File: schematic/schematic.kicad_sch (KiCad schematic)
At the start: 0 parts

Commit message: a
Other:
- title: (none) -> Overview
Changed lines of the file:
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@@
 (kicad_sch (version 20211123) (generator eeschema)
   (paper "USLetter")
+  (title_block
+    (title "Overview")
+    (date "2022-03-18")
+    (comment 1 "Engineer/Draftsman: Joesphan Lu")
+  )
   (junction (at 82.55 49.53) (diameter 0) (color 0 0 0 0)
   )
@@
       (reference "#PWR0178") (unit 1) (value "GND") (footprint "")
     )
+    (path "/00000000-0000-0000-0000-00006200d680/56a155f6-67fb-4ed4-abee-b01de92744a0"
+      (reference "#PWR?") (unit 1) (value "Vdrive") (footprint "")
+    )
     (path "/00000000-0000-0000-0000-000061f58c1a/00000000-0000-0000-0000-000062198c67"

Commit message: e
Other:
- sheet MCU ports: added DRIVER; removed DRIVER_P, MOS_VDRIVE_PWM
- sheet Peltier Driver ports: added DRIVER; removed CHG_PUMP_PWM, DRIVER_N, DRIVER_P
- sheet Power Management ports: added 5V; removed none

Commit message: d
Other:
- sheet ports renamed Human Interface
- sheet Human Interface: file ports.kicad_sch -> HI.kicad_sch
- sheet Human Interface ports: added none; removed PELTIER_N, PELTIER_P
- sheet MCU ports: added ~DRIVER_DIR, ~DRIVER_EN; removed DRIVER, DRIVER_N
- sheet Peltier Driver ports: added 5V, ~DRIVER_DIR, ~DRIVER_EN; removed DRIVER, MOS_VDRIVE, PELTIER_N, PELTIER_P

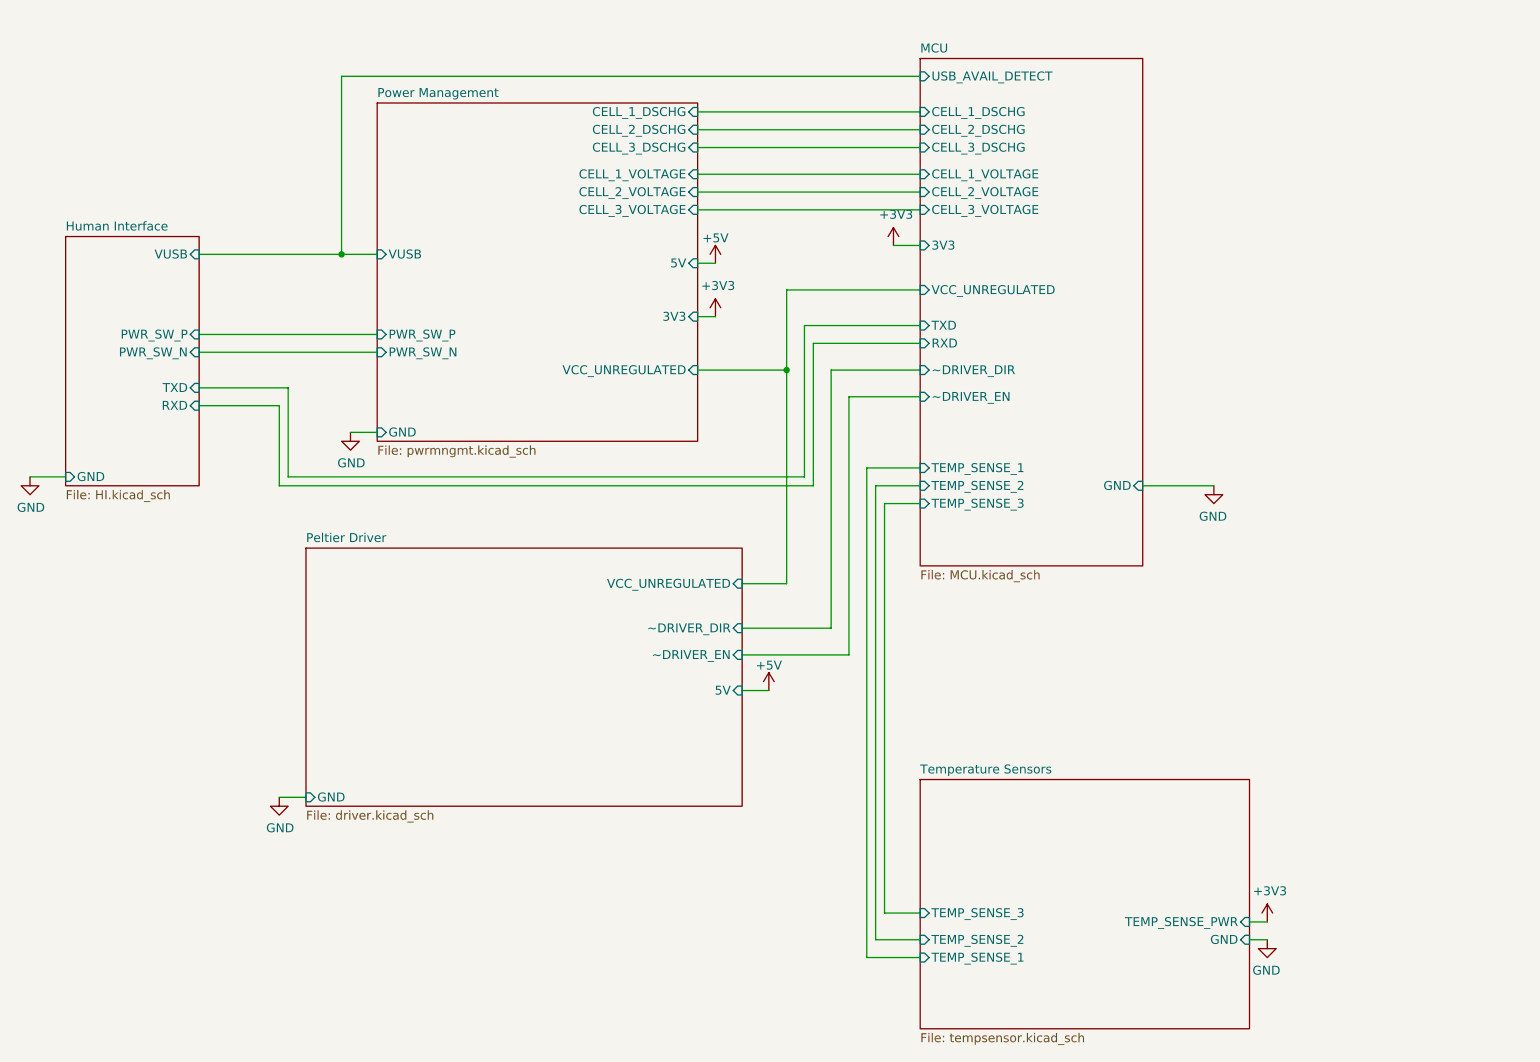
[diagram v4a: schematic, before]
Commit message: beta boards routed
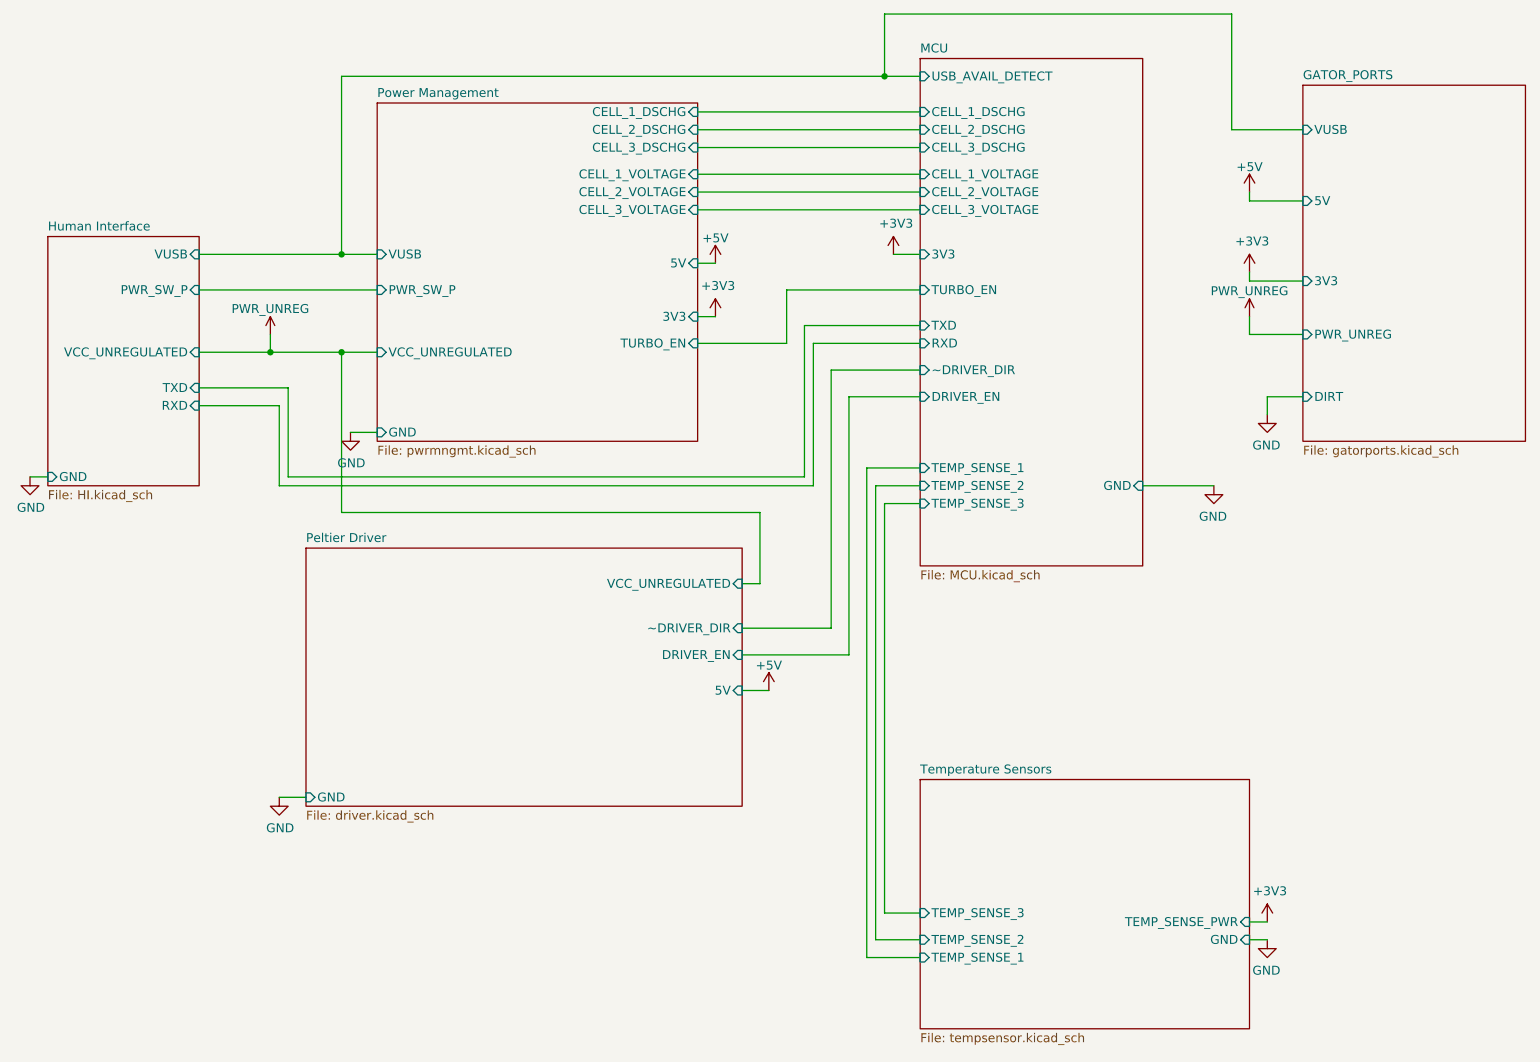
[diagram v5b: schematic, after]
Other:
- added sheet GATOR_PORTS (gatorports.kicad_sch)
- sheet Human Interface ports: added VCC_UNREGULATED; removed PWR_SW_N
- sheet MCU ports: added DRIVER_EN, TURBO_EN; removed VCC_UNREGULATED, ~DRIVER_EN
- sheet Peltier Driver ports: added DRIVER_EN; removed ~DRIVER_EN
- sheet Power Management ports: added TURBO_EN; removed PWR_SW_N

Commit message: prelim ble working
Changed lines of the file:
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@@
   (junction (at 72.39 63.5) (diameter 0) (color 0 0 0 0)
   )
-  (junction (at 82.55 63.5) (diameter 0) (color 0 0 0 0)
-  )
   (junction (at 160.02 24.13) (diameter 0) (color 0 0 0 0)
   )
@@
     (stroke (width 0) (type default) (color 0 0 0 0))
   )
-  (wire (pts (xy 87.63 63.5) (xy 82.55 63.5))
-    (stroke (width 0) (type default) (color 0 0 0 0))
-  )
-  (wire (pts (xy 74.93 68.58) (xy 74.93 81.28))
-    (stroke (width 0) (type default) (color 0 0 0 0))
-  )
-  (wire (pts (xy 149.86 82.55) (xy 73.66 82.55))
+  (wire (pts (xy 69.85 68.58) (xy 69.85 81.28))
+    (stroke (width 0) (type default) (color 0 0 0 0))
+  )
+  (wire (pts (xy 149.86 82.55) (xy 67.31 82.55))
     (stroke (width 0) (type default) (color 0 0 0 0))
   )
@@
     (stroke (width 0) (type default) (color 0 0 0 0))
   )
-  (wire (pts (xy 142.24 86.36) (xy 82.55 86.36))
-    (stroke (width 0) (type default) (color 0 0 0 0))
-  )
   (wire (pts (xy 149.86 62.23) (xy 149.86 82.55))
     (stroke (width 0) (type default) (color 0 0 0 0))
@@
     (stroke (width 0) (type default) (color 0 0 0 0))
   )
-  (wire (pts (xy 73.66 82.55) (xy 73.66 71.12))
+  (wire (pts (xy 67.31 82.55) (xy 67.31 71.12))
     (stroke (width 0) (type default) (color 0 0 0 0))
   )
@@
     (stroke (width 0) (type default) (color 0 0 0 0))
   )
-  (wire (pts (xy 74.93 81.28) (xy 148.59 81.28))
-    (stroke (width 0) (type default) (color 0 0 0 0))
-  )
-  (wire (pts (xy 73.66 71.12) (xy 62.23 71.12))
+  (wire (pts (xy 69.85 81.28) (xy 148.59 81.28))
+    (stroke (width 0) (type default) (color 0 0 0 0))
+  )
+  (wire (pts (xy 67.31 71.12) (xy 62.23 71.12))
     (stroke (width 0) (type default) (color 0 0 0 0))
   )
@@
     (stroke (width 0) (type default) (color 0 0 0 0))
   )
-  (wire (pts (xy 142.24 96.52) (xy 139.7 96.52))
-    (stroke (width 0) (type default) (color 0 0 0 0))
-  )
   (wire (pts (xy 212.09 147.32) (xy 214.63 147.32))
     (stroke (width 0) (type default) (color 0 0 0 0))
@@
     (stroke (width 0) (type default) (color 0 0 0 0))
   )
+  (wire (pts (xy 72.39 96.52) (xy 77.47 96.52))
+    (stroke (width 0) (type default) (color 0 0 0 0))
+  )
   (wire (pts (xy 135.89 58.42) (xy 133.35 58.42))
     (stroke (width 0) (type default) (color 0 0 0 0))
@@
     (stroke (width 0) (type default) (color 0 0 0 0))
   )
-  (wire (pts (xy 82.55 86.36) (xy 82.55 63.5))
+  (wire (pts (xy 72.39 63.5) (xy 72.39 96.52))
     (stroke (width 0) (type default) (color 0 0 0 0))
   )
@@
     (stroke (width 0) (type default) (color 0 0 0 0))
   )
-  (wire (pts (xy 72.39 63.5) (xy 82.55 63.5))
+  (wire (pts (xy 72.39 63.5) (xy 87.63 63.5))
     (stroke (width 0) (type default) (color 0 0 0 0))
   )
@@
     (stroke (width 0) (type default) (color 0 0 0 0))
   )
-  (wire (pts (xy 62.23 68.58) (xy 74.93 68.58))
+  (wire (pts (xy 62.23 68.58) (xy 69.85 68.58))
     (stroke (width 0) (type default) (color 0 0 0 0))
   )
@@
   )
   (wire (pts (xy 62.23 63.5) (xy 72.39 63.5))
-    (stroke (width 0) (type default) (color 0 0 0 0))
-  )
-  (wire (pts (xy 142.24 96.52) (xy 142.24 86.36))
     (stroke (width 0) (type default) (color 0 0 0 0))
   )
@@
       (effects (font (size 1.27 1.27)) (justify left top))
     )
-    (pin "VCC_UNREGULATED" input (at 139.7 96.52 0)
-      (effects (font (size 1.27 1.27)) (justify right))
+    (pin "VCC_UNREGULATED" input (at 77.47 96.52 180)
+      (effects (font (size 1.27 1.27)) (justify left))
     )
     (pin "GND" input (at 77.47 127 180)

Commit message: e
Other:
- sheet MCU ports: added none; removed TURBO_EN
- sheet Power Management ports: added none; removed TURBO_EN

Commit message: e
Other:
- sheet Human Interface ports: added 3V3, EN, IO0; removed none
- sheet MCU ports: added DRIVER_DIR, EN, IO0; removed ~DRIVER_DIR
- sheet Peltier Driver ports: added DRIVER_DIR; removed ~DRIVER_DIR
